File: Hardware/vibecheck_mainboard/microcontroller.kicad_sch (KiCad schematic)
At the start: 36 parts, among them J201 Conn_01x04_Socket, J202 Conn_02x06, J204 TC2030-NL, Q201 BSS138, Q202 BSS138, Q203 BSS138, SW201 SW_Push, U201 STM32H723VGTx, Y201 24MHz

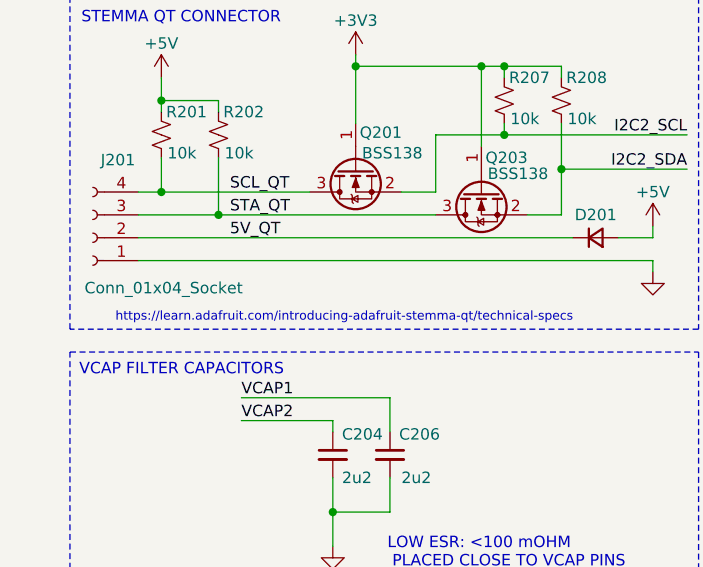
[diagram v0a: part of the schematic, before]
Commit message: VibeCheck mainboard V1.1 sent to JLCPCB
Changes made to main board:
- audio filter/amplifier gain changed from 1.5 to 1. Changed values of R_in and R_f resistors.
- changed sensor labels on board from 'accel 1' ... to 'sensor 0' ... to match firmware
- updated BOM and DNP parts to make sure they matched better reducing warnings in JLCPCB parts selection process
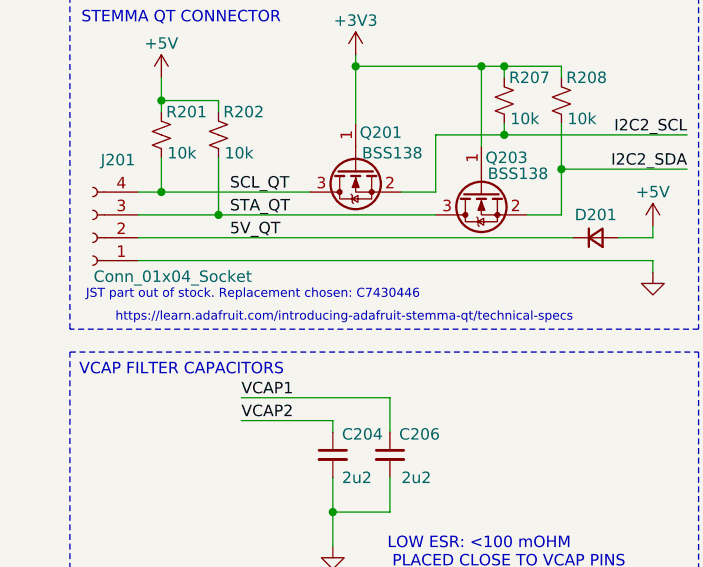
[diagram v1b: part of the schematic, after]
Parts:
- J202, TP201, TP202, TP203, TP204: now left out of the parts list
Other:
- note added: "JST part out of stock. Replacement chosen: C7430446"
